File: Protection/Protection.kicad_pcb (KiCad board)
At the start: 2 copper layers, 65 x 80 mm, 71 parts, among them J1 V_IN, J2 JST_02, J3 5V_IN, J4 V_OUT, J5 JST_07, J6 JST_02, Q1 2N3904, Q2 BT152-800R, Q3 2N3904, Q4 2N3904, Q5 2N3904, Q6 IRF1404/IRFB4110, Q8 IRF1404/IRFB4110, U1 TL431LP, U2 LM393, U3 TLP250

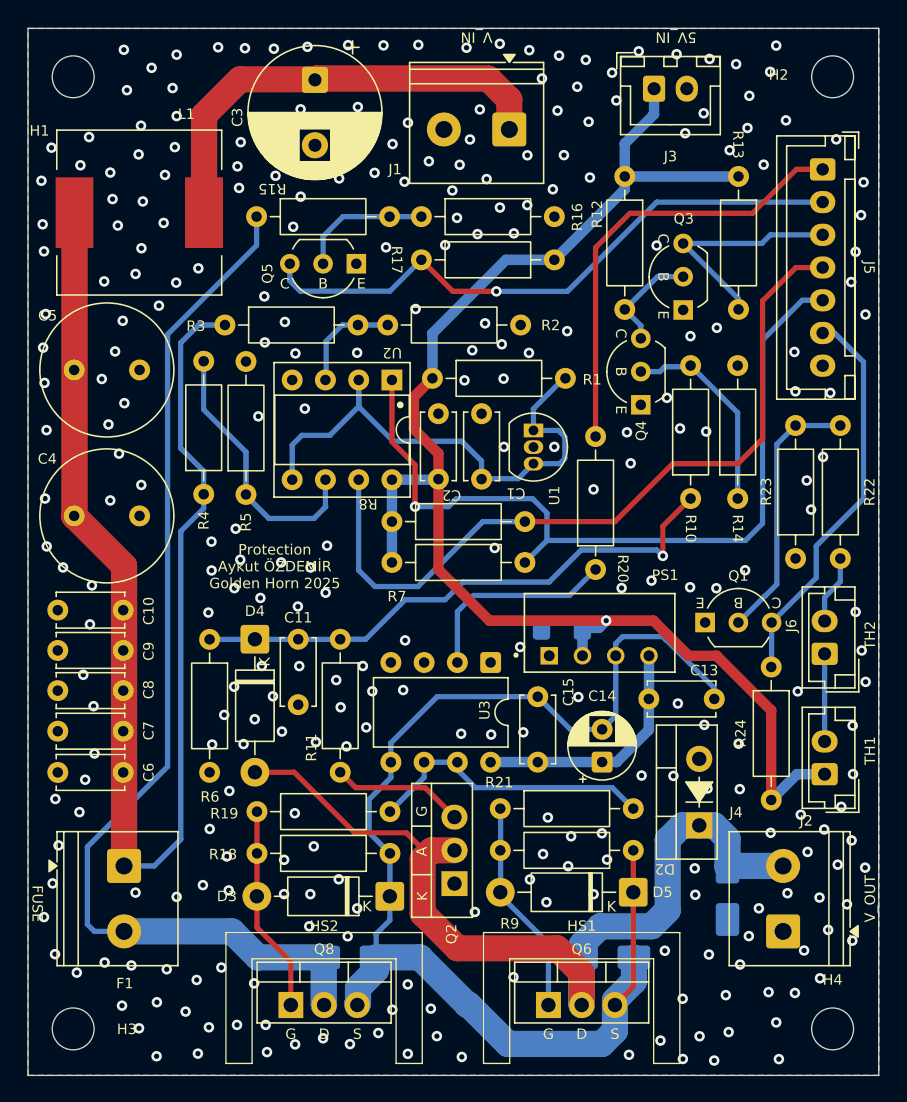
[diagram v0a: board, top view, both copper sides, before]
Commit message: Undervoltage protection fixed for adj ch
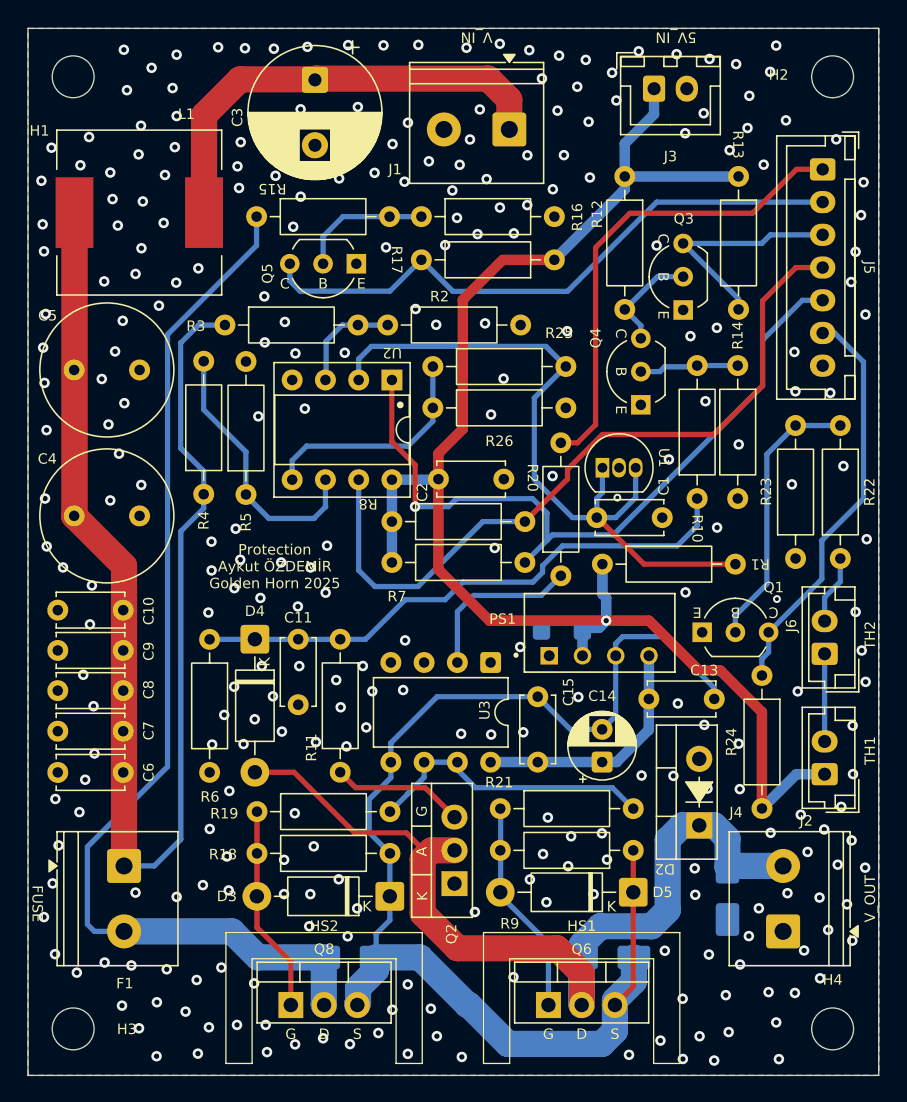
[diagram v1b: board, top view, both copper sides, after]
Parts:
- added R25: 0/0/0/10k, Resistor_THT:R_Axial_DIN0207_L6.3mm_D2.5mm_P10.16mm_Horizontal, F.Cu at (108.5, 92.0)
- added R26: NC/NC/NC/3k9, Resistor_THT:R_Axial_DIN0207_L6.3mm_D2.5mm_P10.16mm_Horizontal, F.Cu at (108.5, 95.1)
- R4: value 30k/120k/330k/360k -> 30k/120k/330k/1k
- R5: value 150k/150k/100k/47k -> 150k/150k/100k/3V Zener
- moved R1 19.2 mm to (121.4, 107.1)
- moved R14 10.2 mm to (131.8, 91.9), turned to -90 degrees
- moved C1 9.28 mm to (121.0, 103.5), turned to 0 degrees
- moved U1 5.99 mm to (121.4, 99.7), turned to 0 degrees
- moved R20 2.70 mm to (118.2, 108.0)
- moved R24 0.96 mm to (133.6, 115.6)
- moved Q1 0.78 mm to (129.0, 112.3)
- moved R10 0.50 mm to (128.7, 102.0)
- turned C2 to 0 degrees
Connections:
- U2 pad 5: Net-(C1-+) -> Net-(R25-+)
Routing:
- net Net-(R25-+): track 0.00 -> 17.6 mm
- net Net-(C1-+): track 41.7 -> 56.0 mm
- net Net-(Q4-B): track 15.5 -> 6.96 mm
- net /OverVoltage: track 62.5 -> 56.4 mm
- net +5V: track 111.6 -> 115.5 mm
- net Net-(R20-+): track 15.8 -> 12.9 mm
- net ON_OFF: track 34.3 -> 36.6 mm
- net /UnderVoltage: track 59.2 -> 57.2 mm
- net FN: track 30.2 -> 31.2 mm
- net Net-(Q1-B): track 20.3 -> 21.1 mm
- net Net-(C11-+): track 42.9 -> 43.2 mm, vias 1 -> 0
- net GND: vias 299 -> 292
- net /FuseBlow: vias 1 -> 0
